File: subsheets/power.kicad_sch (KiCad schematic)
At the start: 30 parts, among them J1 USB_B_Micro, U1 MCP73871_U, U2 LP2985-3.3

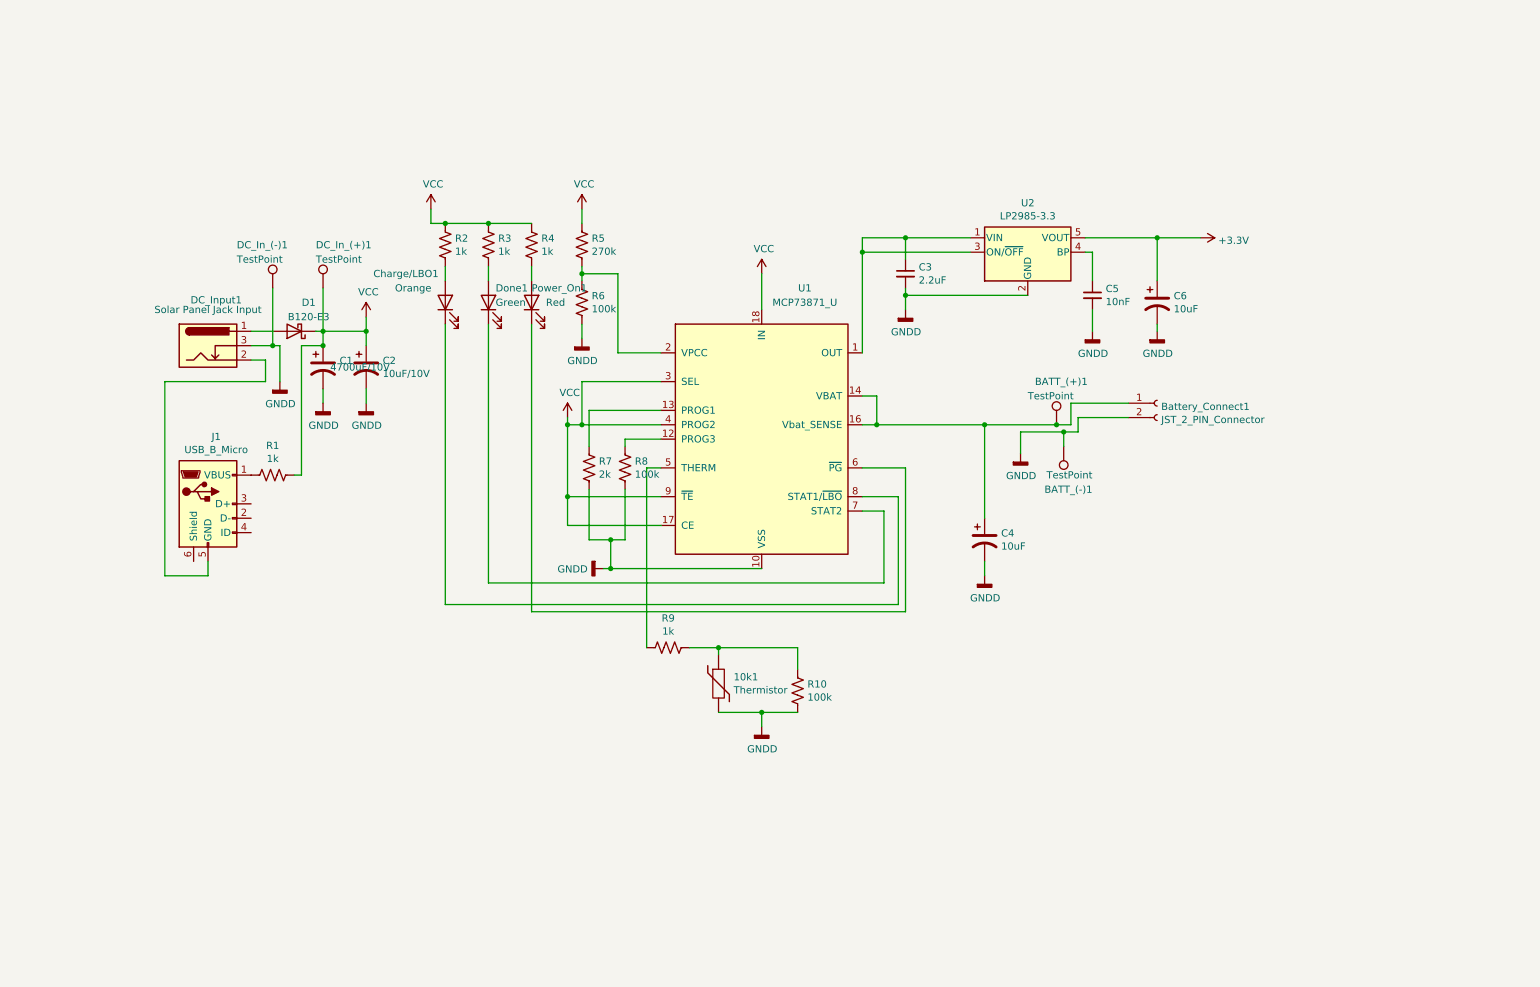
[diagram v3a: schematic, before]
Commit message: USB Comm Interface complete; Sensor and MCU connection complete;
-
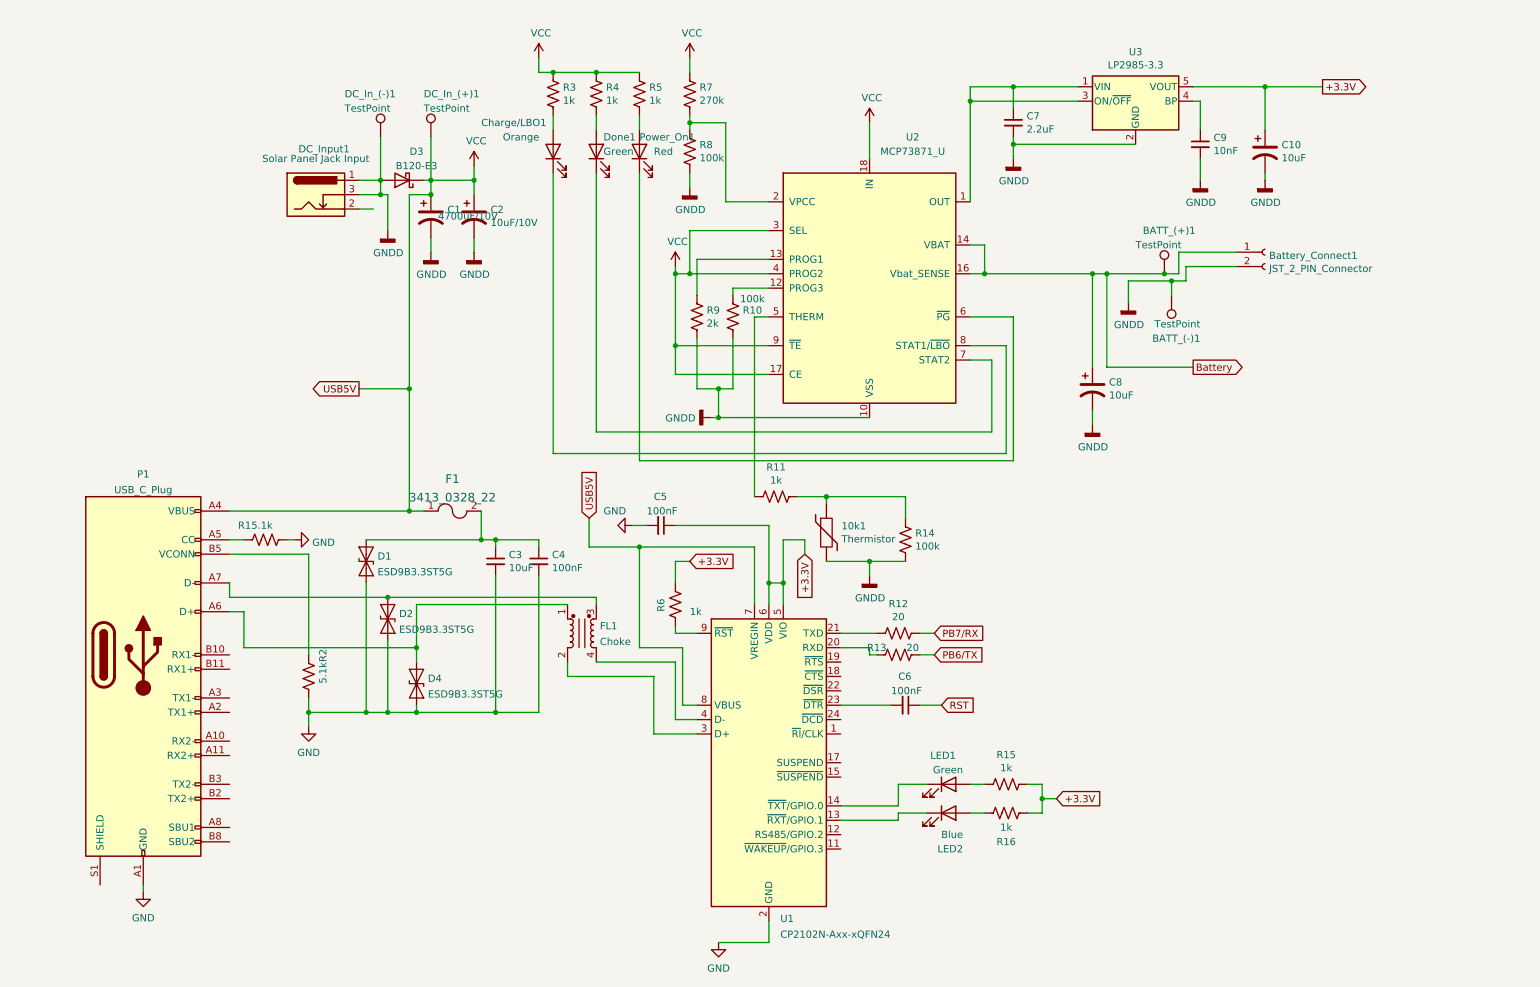
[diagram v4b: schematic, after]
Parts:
- removed J1: USB_B_Micro, symbol Connector:USB_B_Micro
- added C3: 10uF, symbol Device:C_Small
- added C4, C5, C6: 100nF, symbol Device:C_Small
- added D1, D2, D4: ESD9B3.3ST5G, Diode_SMD:D_SOD-923, symbol Diode:ESD9B3.3ST5G
- added F1: 3413_0328_22, digikey-footprints:1206, symbol dk_Fuses:3413_0328_22
- added FL1: Choke, symbol Device:Filter_EMI_CommonMode
- added LED1: Green, symbol Device:LED
- added LED2: Blue, symbol Device:LED
- added P1: USB_C_Plug, symbol Connector:USB_C_Plug
- added R12, R13: 20, symbol Device:R_US
- added R15, R16, R6: 1k, symbol Device:R_US
- added R2: 5.1k, symbol Device:R_US
- added U1: CP2102N-Axx-xQFN24, Package_DFN_QFN:QFN-24-1EP_4x4mm_P0.5mm_EP2.6x2.6mm, symbol Interface_USB:CP2102N-Axx-xQFN24
- R1: value 1k -> 5.1k
- renumbered C6 to C10, C3 to C7, C4 to C8, C5 to C9, D1 to D3, R8 to R10, R9 to R11, R10 to R14, R2 to R3, R3 to R4, R4 to R5, R5 to R7, R6 to R8, R7 to R9, U1 to U2, U2 to U3
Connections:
- net GNDD: now also D3.2 (A), DC_Input1.1
- net VCC: now also F1.1, P1.A4 (VBUS), P1.A9 (VBUS), P1.B4 (VBUS), P1.B9 (VBUS), U1.7 (VREGIN), U1.8 (VBUS); no longer R1.1
- net Battery: now reaches BATT_(+)1.1, Battery_Connect1.1 (Pin_1), C8.1, U2.14 (VBAT), U2.15 (VBAT), U2.16 (Vbat_SENSE)
- net at R1.2: now also P1.A5 (CC)
- net +3V3 renamed +3.3V
- net +3.3V: now also C5.1, R15.1, R16.1, R6.2, U1.5 (VIO), U1.6 (VDD)
- new net: LED2.1 (K), U1.13 (~{RXT}/GPIO.1)
- new net: LED1.1 (K), U1.14 (~{TXT}/GPIO.0)
- new net: R13.2, U1.20 (RXD)
- new net: R12.2, U1.21 (TXD)
- new net: C6.2, U1.23 (~{DTR})
- new net: FL1.2, U1.3 (D+)
- new net: FL1.4, U1.4 (D-)
- new net: R6.1, U1.9 (~{RST})
- new net: LED2.2 (A), R16.2
- new net: D4.1 (A1), FL1.1, P1.A6 (D+)
- new net: D2.1 (A1), FL1.3, P1.A7 (D-)
- new net: P1.B5 (VCONN), R2.2
- new net: LED1.2 (A), R15.2
- new net: C3.1, C4.1, D1.1 (A1), F1.2
- new net GND: C3.2, C4.2, C5.2, D1.2 (A2), D2.2 (A2), D4.2 (A2), P1.A1 (GND), P1.A12 (GND), P1.B1 (GND), P1.B12 (GND), R1.1, R2.1, U1.2 (GND), U1.25 (GND)
- new net PB6/TX: R13.1
- new net PB7/RX: R12.1
- new net RST: C6.1
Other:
- moved on the sheet: 10k1, BATT_(+)1, BATT_(-)1, Battery_Connect1, C1, C10, C2, C7, C8, C9, Charge/LBO1, D3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

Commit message: A few schematic changes and fixes
-
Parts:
- removed F1: 3413_0328_22, digikey-footprints:1206, symbol dk_Fuses:3413_0328_22
- added C12: 10uF, symbol Device:C_Small
- added C9: 1uF, symbol Device:C_Small
- added F1: 1A, symbol Device:Polyfuse_Small
- added L1: 10uH, symbol Device:L
- added R15: 10k, symbol Device:R_US
- added U4: LTC3525-5, Package_TO_SOT_SMD:SOT-363_SC-70-6, symbol Regulator_Switching:LTC3525-5
- D1, D4: value ESD9B3.3ST5G -> ESD Diode
- D3: renamed from D2; value ESD9B3.3ST5G -> ESD Diode
- renumbered C9 to C10, C10 to C11, D3 to D2, R12 to R11, R13 to R12, R15 to R13, R16 to R14, R11 to R16, R14 to R17
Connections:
- net +3.3V: no longer C5.1, R13.1, R14.1, R6.2, U1.5 (VIO), U1.6 (VDD)
- net Battery: now also C9.1, L1.1, U4.3 (VIN)
- net GND: now also C12.2, C9.2, R15.2, U4.2 (GND), U4.5 (GND)
- net GNDD: no longer 10k1.2, R17.1
- net VCC: now also C3.1, C4.1, D1.1 (A1), F1.2; no longer P1.A4 (VBUS), P1.A9 (VBUS), P1.B4 (VBUS), P1.B9 (VBUS)
- net THERM: now reaches R16.2, U2.5 (THERM)
- net Power On: now reaches Power_On1.1 (K), U2.6 (~{PG})
- net Charge Done: now reaches Done1.1 (K), U2.7 (STAT2)
- net Charge/LBO : now reaches Charge/LBO1.1 (K), U2.8 (STAT1/~{LBO})
- net at U1.3 (D+): no longer FL1.2
- new net: P1.A4 (VBUS), P1.A9 (VBUS), P1.B4 (VBUS), P1.B9 (VBUS)
- new net: L1.2, U4.6 (SW)
- new net +5V: C12.1, U4.4 (VOUT)
- new net Boost SHDN/PC1: R15.1, U4.1 (~{SHDN})
- new net GNDS: 10k1.2, R17.1
- new net VDD: C5.1, R13.1, R14.1, R6.2, U1.5 (VIO), U1.6 (VDD)
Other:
- moved on the sheet: 10k1, C3, C4, D1, D3, D4, FL1, R16, R17, R2

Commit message: -
-
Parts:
- added 5V(+), 5V(-): TestPoint, TestPoint:TestPoint_Keystone_5005-5009_Compact, symbol Connector:TestPoint
- BATT_(+)1, BATT_(-)1, DC_In_(+)1, DC_In_(-)1: footprint (none) -> TestPoint:TestPoint_Keystone_5005-5009_Compact
- R3: footprint (none) -> Resistor_SMD:R_0805_2012Metric_Pad1.20x1.40mm_HandSolder
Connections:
- net +5V: now also 5V(+).1
- net GND: now also 5V(-).1
- net GNDD: no longer D2.2 (A), DC_Input1.1
- new net: D2.2 (A), DC_Input1.1
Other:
- moved on the sheet: DC_In_(-)1

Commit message: USB updated. All footprints added for the most part
-
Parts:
- removed P1: USB_C_Plug, symbol Connector:USB_C_Plug
- added 3.3V(+), 3.3V(-), D+, D-, USB_5V+: TestPoint, TestPoint:TestPoint_Keystone_5005-5009_Compact, symbol Connector:TestPoint
- added J?: USB_C_Receptacle_USB2.0, Connector_USB:USB_C_Receptacle_Amphenol_12401610E4-2A, symbol Connector:USB_C_Receptacle_USB2.0
- C1, C10, C11, C12, C2, C3, C4, C5, C6, C7, C8, C9: footprint (none) -> Capacitor_SMD:C_0805_2012Metric_Pad1.18x1.45mm_HandSolder
- FL1: footprint (none) -> Inductor_SMD:L_CommonModeChoke_Coilcraft_0805USB
- R1, R10, R11, R12, R13, R14, R15, R16, R17, R4, R5, R6, R7, R8, R9: footprint (none) -> Resistor_SMD:R_0805_2012Metric_Pad1.20x1.40mm_HandSolder
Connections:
- net +3.3V: now also 3.3V(+).1
- net GND: now also J?.A1 (GND), J?.A12 (GND), J?.B1 (GND), J?.B12 (GND), J?.S1 (SHIELD)
- net GNDD: now also 3.3V(-).1
- net VCC: now also USB_5V+.1
- net at U1.3 (D+): now also FL1.2
- net at D4.1 (A1), FL1.1: now also D+.1, J?.B6 (D+)
- net at D3.1 (A1), FL1.3: now also D-.1, J?.B7 (D-)
- net at R2.2: now also J?.B5 (CC2)
- net at R1.2: now also J?.A5 (CC1)
- net at F1.1: now also J?.A4 (VBUS), J?.A9 (VBUS), J?.B4 (VBUS), J?.B9 (VBUS)

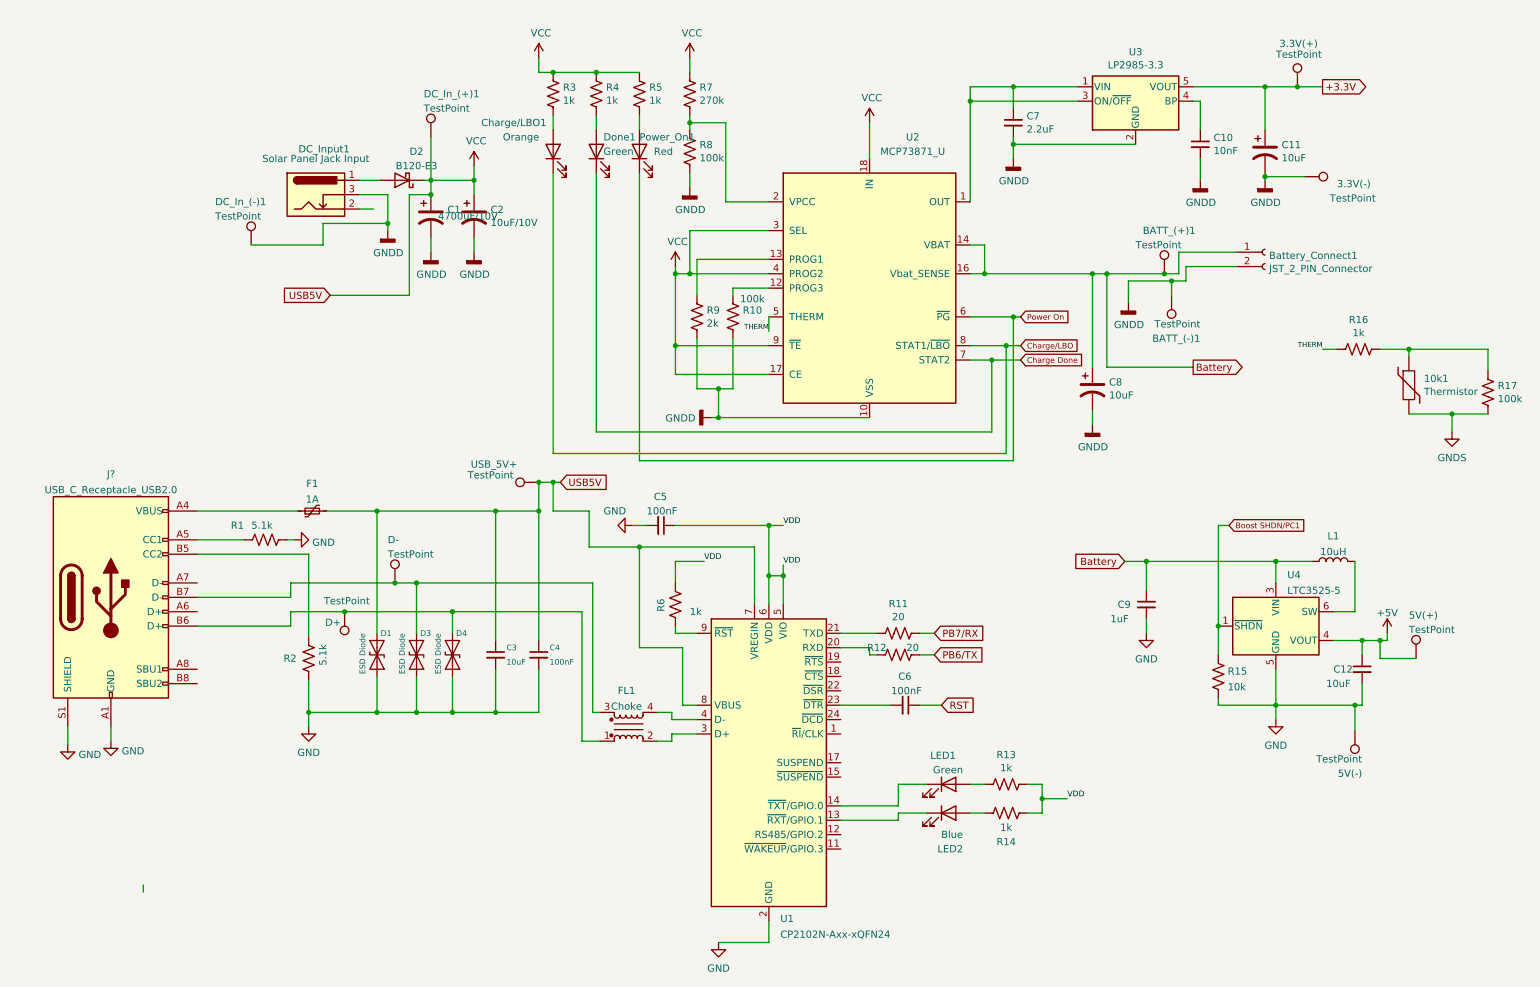
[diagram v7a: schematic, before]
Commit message: Some schematic changes. Preliminary PCB layout complete, routing not done yet
-
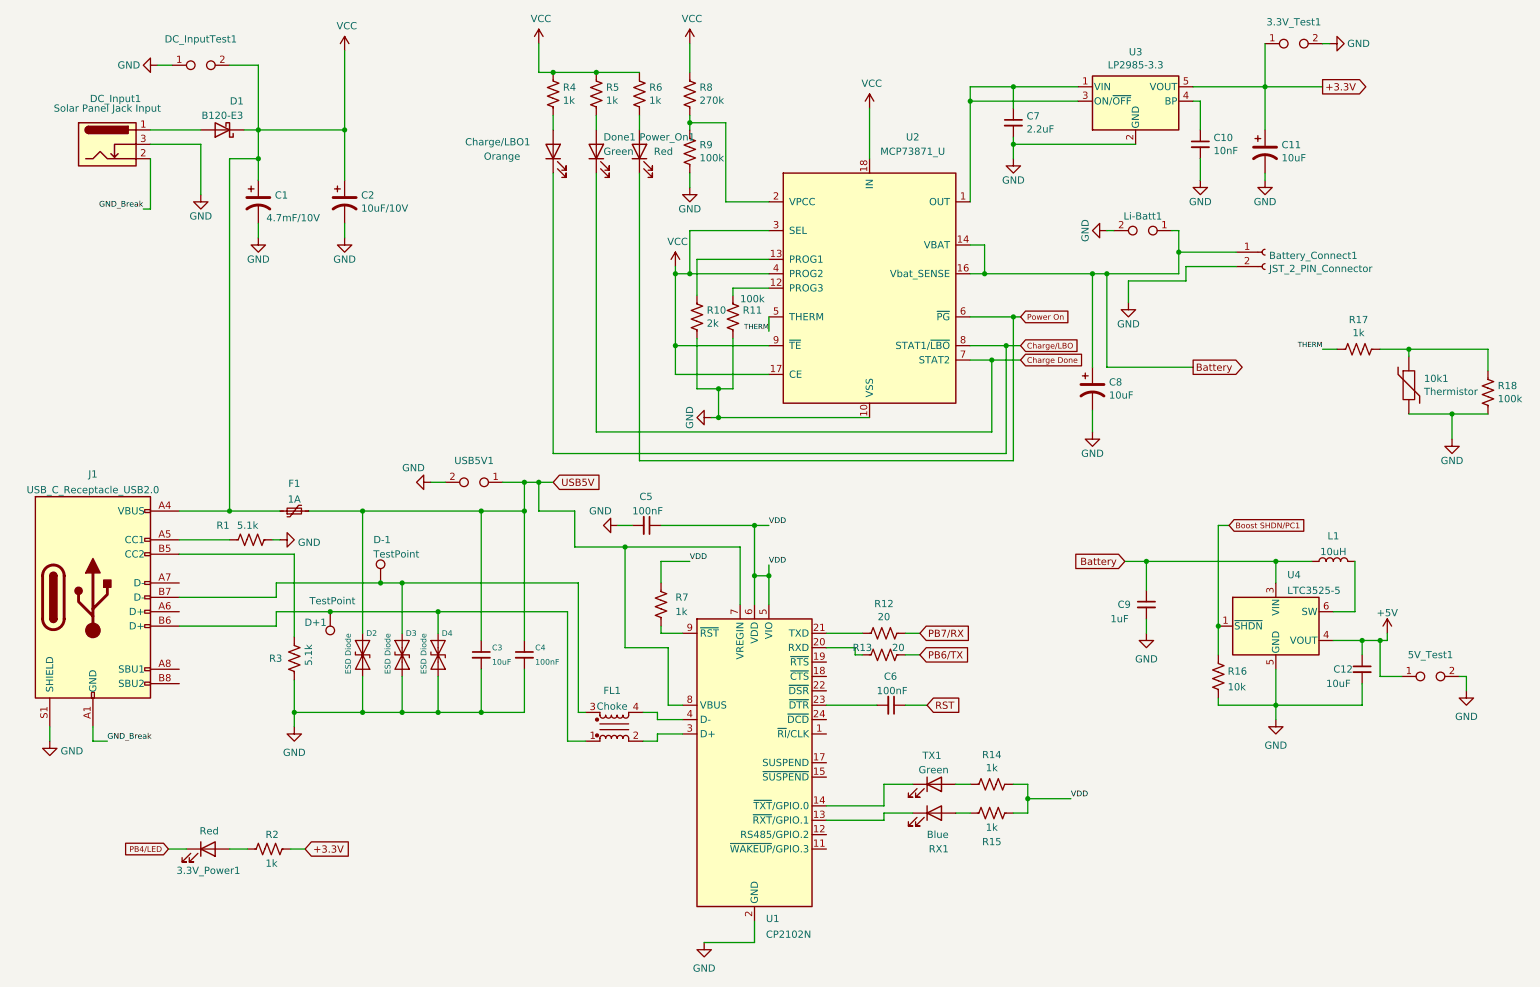
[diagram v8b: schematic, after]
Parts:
- removed 3.3V(+), 3.3V(-), 5V(+), 5V(-), BATT_(+)1, BATT_(-)1, DC_In_(+)1, DC_In_(-)1, USB_5V+: TestPoint, TestPoint:TestPoint_Keystone_5005-5009_Compact, symbol Connector:TestPoint
- added 3.3V_Power1: Red, LED_SMD:LED_0805_2012Metric_Pad1.15x1.40mm_HandSolder, symbol Device:LED
- added 3.3V_Test1, 5V_Test1, DC_InputTest1, Li-Batt1, USB5V1: TestPoint, TestPoint:TestPoint_2Pads_Pitch2.54mm_Drill0.8mm, symbol Connector:TestPoint_2Pole
- added R2: 1k, Resistor_SMD:R_0805_2012Metric_Pad1.20x1.40mm_HandSolder, symbol Device:R_US
- 10k1: footprint (none) -> TerminalBlock:TerminalBlock_Altech_AK300-2_P5.00mm
- Battery_Connect1: footprint (none) -> Connector_JST:JST_PH_B2B-PH-SM4-TB_1x02-1MP_P2.00mm_Vertical
- C1: value 4700uF/10V -> 4.7mF/10V; footprint Capacitor_SMD:C_0805_2012Metric_Pad1.18x1.45mm_HandSolder -> Capacitor_THT:CP_Radial_D13.0mm_P5.00mm
- Charge/LBO1, Done1, Power_On1: footprint (none) -> LED_SMD:LED_0805_2012Metric_Pad1.15x1.40mm_HandSolder
- D+1: renamed from D+; footprint TestPoint:TestPoint_Keystone_5005-5009_Compact -> TestPoint:TestPoint_Keystone_5000-5004_Miniature
- D-1: renamed from D-; footprint TestPoint:TestPoint_Keystone_5005-5009_Compact -> TestPoint:TestPoint_Keystone_5000-5004_Miniature
- D2: renamed from D1; footprint Diode_SMD:D_SOD-923 -> Diode_SMD:D_0402_1005Metric_Pad0.77x0.64mm_HandSolder
- D3, D4: footprint Diode_SMD:D_SOD-923 -> Diode_SMD:D_0402_1005Metric_Pad0.77x0.64mm_HandSolder
- DC_Input1: footprint (none) -> Connector_BarrelJack:BarrelJack_Horizontal
- F1: footprint (none) -> Fuse:Fuse_0805_2012Metric_Pad1.15x1.40mm_HandSolder
- L1: footprint (none) -> Inductor_SMD:L_0805_2012Metric_Pad1.15x1.40mm_HandSolder
- R3: renamed from R2; footprint (none) -> Resistor_SMD:R_0805_2012Metric_Pad1.20x1.40mm_HandSolder
- RX1: renamed from LED2; footprint (none) -> LED_SMD:LED_0805_2012Metric_Pad1.15x1.40mm_HandSolder
- TX1: renamed from LED1; footprint (none) -> LED_SMD:LED_0805_2012Metric_Pad1.15x1.40mm_HandSolder
- U1: value CP2102N-Axx-xQFN24 -> CP2102N
- gave numbers to parts that had none: 1
- renumbered D2 to D1, R9 to R10, R10 to R11, R11 to R12, R12 to R13, R13 to R14, R14 to R15, R15 to R16, R16 to R17, R17 to R18, R3 to R4, R4 to R5, R5 to R6, R6 to R7, R7 to R8, R8 to R9
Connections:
- net GNDD is gone; now on net GND: Battery_Connect1.2 (Pin_2), C1.2, C10.2, C11.2, C2.2, C7.2, C8.2, DC_Input1.3, R10.1, R11.1, R9.1, U2.10 (VSS), U2.11 (VSS), U2.21 (VSS), U3.2 (GND)
- net GNDS is gone; now on net GND: 10k1.2, R18.1
- net +3.3V: now also 3.3V_Test1.1, R2.2
- net +5V: now also 5V_Test1.1
- net Battery: now also Li-Batt1.1
- net GND: now also 3.3V_Test1.2, 5V_Test1.2, DC_InputTest1.1, Li-Batt1.2, USB5V1.2; no longer J1.A1 (GND), J1.A12 (GND), J1.B1 (GND), J1.B12 (GND)
- net VCC: now also F1.1, J1.A4 (VBUS), J1.A9 (VBUS), J1.B4 (VBUS), J1.B9 (VBUS), DC_InputTest1.2; no longer C3.1, C4.1, D2.1 (A1), F1.2, U1.7 (VREGIN), U1.8 (VBUS)
- net GND_Break: now reaches DC_Input1.2
- net GND_Break: now also J1.A1 (GND), J1.A12 (GND), J1.B1 (GND), J1.B12 (GND)
- new net: 3.3V_Power1.2 (A), R2.1
- new net PB4/LED: 3.3V_Power1.1 (K)
- new net USB5V: C3.1, C4.1, D2.1 (A1), F1.2, U1.7 (VREGIN), U1.8 (VBUS), USB5V1.1
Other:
- moved on the sheet: C1, C2, C3, C4, C5, C6, D+1, D-1, D1, D2, D3, D4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
